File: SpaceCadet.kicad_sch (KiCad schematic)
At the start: 35 parts, among them J0 Conn_02x17_Odd_Even, J3_1 Conn_01x04, J3_2 Conn_01x04, U1 74LS154, U2 8048, Y3 Crystal 3.58MHz

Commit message: RP2040 added
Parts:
- added BOOT1, RST1: SW_Push, Button_Switch_SMD:SW_SPST_TL3342, symbol Switch:SW_Push
- added C1, C12, C2, C4, C6: 1u, Capacitor_SMD:C_0402_1005Metric, symbol Device:C_Small
- added C10, C11: 22p, Capacitor_SMD:C_0402_1005Metric, symbol Device:C_Small
- added C101: 100n, Button_Switch_SMD:SW_SPST_TL3342, symbol Device:C_Small
- added C3: 10u, Capacitor_SMD:C_0603_1608Metric, symbol Device:C_Small
- added C5, C7, C8: 100n, Capacitor_SMD:C_0402_1005Metric, symbol Device:C_Small
- added F17: Fuse_Small, Fuse:Fuse_1206_3216Metric, symbol Device:Fuse_Small
- added J1: USB_C_Receptacle_USB2.0_16P, Connector_USB:USB_C_Receptacle_HRO_TYPE-C-31-M-12, symbol Connector:USB_C_Receptacle_USB2.0_16P
- added J2: Conn_01x04, Connector_JST:JST_SH_SM04B-SRSS-TB_1x04-1MP_P1.00mm_Horizontal, symbol Connector_Generic:Conn_01x04
- added J3: Conn_01x05, Connector_PinHeader_2.54mm:PinHeader_1x05_P2.54mm_Vertical, symbol Connector_Generic:Conn_01x05
- added R1: 5.1k, Connector_PinHeader_2.54mm:PinHeader_1x05_P2.54mm_Vertical, symbol Device:R_Small
- added R2, R3, R8, R9: 5.1k, Resistor_SMD:R_0402_1005Metric, symbol Device:R_Small
- added R4, R5: 27, Resistor_SMD:R_0402_1005Metric, symbol Device:R_Small
- added R6, R7: 1k, Resistor_SMD:R_0402_1005Metric, symbol Device:R_Small
- added U1: RP2040, Package_DFN_QFN:QFN-56-1EP_7x7mm_P0.4mm_EP3.2x3.2mm, symbol MCU_RaspberryPi:RP2040
- added U2: XC6206PxxxMR, Package_TO_SOT_SMD:SOT-23-3, symbol Regulator_Linear:XC6206PxxxMR
- added U3: SRV05-4, Package_TO_SOT_SMD:SOT-23-6, symbol Power_Protection:SRV05-4
- added U4: W25Q128JVS, Package_SO:SOIC-8_5.23x5.23mm_P1.27mm, symbol Memory_Flash:W25Q128JVS
- added Y1: Crystal_GND24, Crystal:Crystal_SMD_3225-4Pin_3.2x2.5mm_HandSoldering, symbol Device:Crystal_GND24
- J103_1: renamed from J3_1; footprint Connector_PinHeader_2.54mm:PinHeader_1x04_P2.54mm_Vertical -> Connector:FanPinHeader_1x04_P2.54mm_Vertical
- J103_2: renamed from J3_2; footprint Connector_PinHeader_2.54mm:PinHeader_1x04_P2.54mm_Vertical -> Connector:FanPinHeader_1x04_P2.54mm_Vertical
- renumbered C12 to C112, C13 to C113, C14 to C114, C15 to C115, C16 to C116, C17 to C117, R4 to R104, R5 to R105, R6 to R106, R7 to R107, R8 to R108, R9 to R109, R10 to R110, R11 to R111, U1 to U101, U2 to U102, Y3 to Y103
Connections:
- net +5V: now also C1.1, F17.2, J2.1 (Pin_1), U2.3 (VI), U3.5 (VP)
- net GND: now also BOOT1.1, C1.2, C10.1, C101.2, C11.1, C12.2, C2.2, C3.2, C4.2, C5.2, C6.2, C7.2, C8.2, J1.A1 (GND), J1.A12 (GND), J1.B1 (GND), J1.B12 (GND), J1.S1 (SHIELD), J2.4 (Pin_4), J3.3 (Pin_3), R1.2, R2.2, RST1.1, U1.19 (TESTEN), U1.57 (GND), U2.1 (GND), U3.2 (VN), U4.4 (GND), Y1.2, Y1.4
- net RESET: now also J3.1 (Pin_1), R3.1, RST1.2, U1.26 (RUN)
- new net: J1.B5 (CC2), R1.1
- new net: J1.A5 (CC1), R2.1
- new net: C11.2, R6.1, Y1.1
- new net: R4.2, U1.47 (USB_DP)
- new net: R8.2, R9.1
- new net: R5.2, U1.46 (USB_DM)
- new net: BOOT1.2, R7.1
- new net +1V1: C4.1, C5.1, U1.23 (DVDD), U1.45 (VREG_VOUT), U1.50 (DVDD)
- new net +3V3: C101.1, C12.1, C2.1, C3.1, C6.1, C7.1, C8.1, J3.2 (Pin_2), R3.2, R9.2, U1.1 (IOVDD), U1.10 (IOVDD), U1.22 (IOVDD), U1.33 (IOVDD), U1.42 (IOVDD), U1.43 (ADC_AVDD), U1.44 (VREG_IN), U1.48 (USB_VDD), U1.49 (IOVDD), U2.2 (VO), U4.8 (VCC)
- new net D+: J1.A6 (D+), J1.B6 (D+), J2.3 (Pin_3), R4.1, U3.1 (IO1)
- new net D-: J1.A7 (D-), J1.B7 (D-), J2.2 (Pin_2), R5.1, U3.3 (IO2)
- new net Q_CLK: U1.52 (QSPI_SCLK), U4.6 (CLK)
- new net Q_IO0: U1.53 (QSPI_SD0), U4.5 (DI(IO0))
- new net Q_IO1: U1.55 (QSPI_SD1), U4.2 (DO(IO1))
- new net Q_IO2: U1.54 (QSPI_SD2), U4.3 (IO2)
- new net Q_IO3: U1.51 (QSPI_SD3), U4.7 (IO3)
- new net Q_SEL: R7.2, R8.1, U1.56 (QSPI_SS), U4.1 (~{CS})
- new net SVC: J3.4 (Pin_4), U1.24 (SWCLK)
- new net SVD: J3.5 (Pin_5), U1.25 (SWD)
- new net VBUS: F17.1, J1.A4 (VBUS), J1.A9 (VBUS), J1.B4 (VBUS), J1.B9 (VBUS)
- new net XIN: C10.2, U1.20 (XIN), Y1.3
- new net XOUT: R6.2, U1.21 (XOUT)
- no-connect marks 8 -> 10
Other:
- moved on the sheet: C112, C113, C114, C115, C116, C117, J0, J103_1, J103_2, JP18, JP19, JP20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

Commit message: wip: pcb updates
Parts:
- added C13, C14, C15, C16: 100n, Capacitor_SMD:C_0402_1005Metric, symbol Device:C_Small
- C12: renamed from C101; footprint Button_Switch_SMD:SW_SPST_TL3342 -> Capacitor_SMD:C_0402_1005Metric
- R1: footprint Connector_PinHeader_2.54mm:PinHeader_1x05_P2.54mm_Vertical -> Resistor_SMD:R_0402_1005Metric
- renumbered C7 to C10, C8 to C11, C10 to C20, C11 to C21, C12 to C5, C4 to C6, C5 to C7, C3 to C8, C6 to C9, R9 to R4, R8 to R5, R7 to R6, R6 to R7, R4 to R94, R5 to R95
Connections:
- net +1V1: now also C13.1
- net +3V3: now also C14.1, C15.1, C16.1
- net GND: now also C13.2, C14.2, C15.2, C16.2
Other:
- moved on the sheet: C10, C11, C12, C8, C9

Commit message: wip: dxf
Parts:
- removed C112, C113, C114: 10pF, TestPoint:Two_Pad_Through_Hole_10.4mm, symbol Device:C
- removed C115: 15pF, TestPoint:Two_Pad_Through_Hole_10.4mm, symbol Device:C_Small
- removed C116: 22uF 15v, TestPoint:Two_Pad_Through_Hole_20mm, symbol Device:C_Polarized_US
- removed C117: 4.7uF 25v, TestPoint:Two_Pad_Through_Hole_12mm, symbol Device:C_Polarized_US
- removed J0: Conn_02x17_Odd_Even, Connector_PinHeader_2.54mm:PinHeader_2x17_P2.54mm_Horizontal, symbol Connector_Generic:Conn_02x17_Odd_Even
- removed J103_1, J103_2: Conn_01x04, Connector:FanPinHeader_1x04_P2.54mm_Vertical, symbol Connector_Generic:Conn_01x04
- removed JP18, JP19, JP23, JP25, JP26, JP27, JP28, JP29, JP30, JP31, JP32: Jumper Open, Jumper:SolderJumper-2_P1.3mm_Open_TrianglePad1.0x1.5mm, symbol Jumper:Jumper_2_Open
- removed JP20, JP21, JP22, JP24: Jumper Bridged, Jumper:SolderJumper-2_P1.3mm_Bridged2Bar_Pad1.0x1.5mm, symbol Jumper:Jumper_2_Bridged
- removed R104, R105, R106, R107, R108, R109, R110, R111: 1K, TestPoint:Two_Pad_Through_Hole_12.4mm, symbol Device:R_US
- removed U101: 74LS154, Package_DIP:DIP-24_W15.24mm_LongPads, symbol 74xx:74LS154
- removed U102: 8048, Package_DIP:DIP-40_W15.24mm_Socket_LongPads, symbol MCU_Intel:8048
- removed Y103: Crystal 3.58MHz, TestPoint:Two_Pad_Through_Hole_10.4mm, symbol Device:Crystal
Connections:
- no-connect marks 10 -> 2
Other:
- note removed: "CLOSED"
- note removed: "Jumper state corresponds to the configuration of the Space Cadet."
- note removed: "OPEN"
- note removed: "TEST POINTS"
- note removed: "[Some references have JP19 bridged.]"

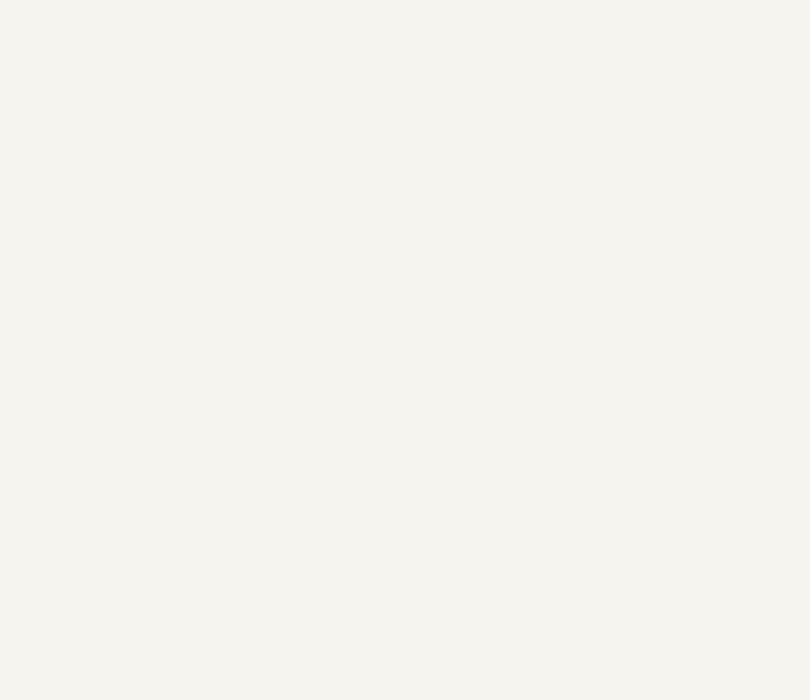
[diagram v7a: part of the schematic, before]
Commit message: wip: display2004 added, fixed to original SpaceCadet layout
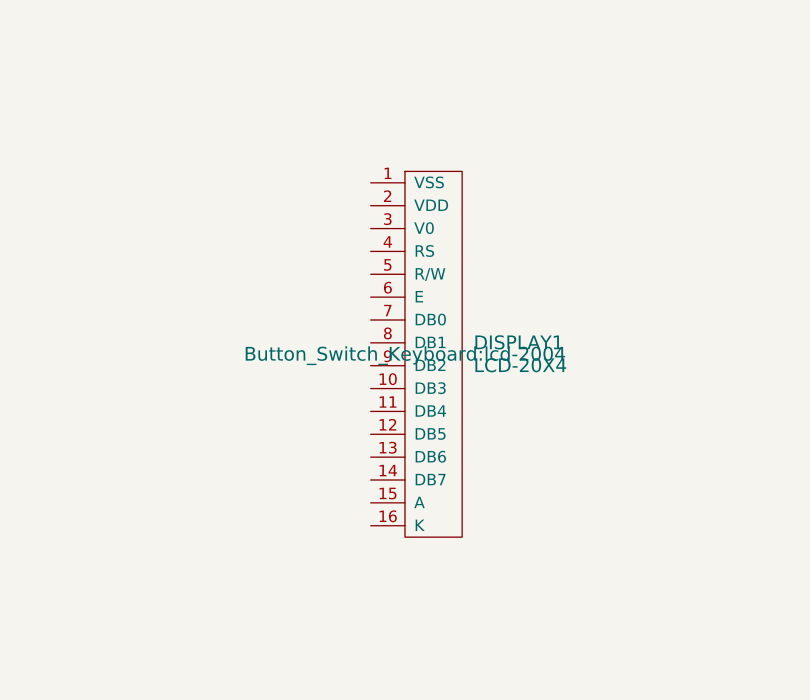
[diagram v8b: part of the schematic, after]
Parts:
- added DISPLAY1: LCD-20X4, Button_Switch_Keyboard:lcd-2004, symbol thinkerforge:LCD-20X4
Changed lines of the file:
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@@
+	)
+	(symbol
+		(lib_id "thinkerforge:LCD-20X4")
+		(at 218.44 303.53 0)
+		(unit 1)
+		(exclude_from_sim no)
+		(in_bom yes)
+		(on_board yes)
+		(dnp no)
+		(fields_autoplaced yes)
+		(property "Reference" "DISPLAY1"
+			(at 226.06 302.2599 0)
+			(effects
+				(font
+					(size 1.524 1.524)
+				)
+				(justify left)
+			)
+		)
+		(property "Value" "LCD-20X4"
+			(at 226.06 304.7999 0)
+			(effects
+				(font
+					(size 1.524 1.524)
+				)
+				(justify left)
+			)
+		)
+		(property "Footprint" "Button_Switch_Keyboard:lcd-2004"
+			(at 218.44 303.53 0)
+			(effects
+				(font
+					(size 1.524 1.524)
+				)
+			)
+		)
+		(property "Datasheet" ""
+			(at 218.44 303.53 0)
+			(effects
+				(font
+					(size 1.524 1.524)
+				)
+			)
+		)
+		(property "Description" ""
+			(at 218.44 303.53 0)
+			(effects
+				(font
+					(size 1.27 1.27)
+				)
+				(hide yes)
+			)
+		)
+		(pin "5"
+		)
+		(pin "2"
+		)
+		(pin "7"
+		)
+		(pin "3"
+		)
+		(pin "4"
+		)
+		(pin "15"
+		)
+		(pin "9"
+		)
+		(pin "12"
+		)
+		(pin "13"
+		)
+		(pin "6"
+		)
+		(pin "14"
+		)
+		(pin "1"
+		)
+		(pin "8"
+		)
+		(pin "16"
+		)
+		(pin "10"
+		)
+		(pin "11"
+		)
+		(instances
+			(project "SpaceCadet"
+				(path "/4f7acbe2-a0f9-477a-99f4-186b01302303"
+					(reference "DISPLAY1")
+					(unit 1)
+				)
+			)
+		)
 	)
 	(symbol
